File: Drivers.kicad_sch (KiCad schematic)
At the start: 15 parts, among them IC1 A3909GLNTR-T, IC2 A3909GLNTR-T, IC3 A3909GLNTR-T, IC4 A3909GLNTR-T, J1 7 Seg Out, J3 Logic I/O, U1 74HC595, U2 74HC595

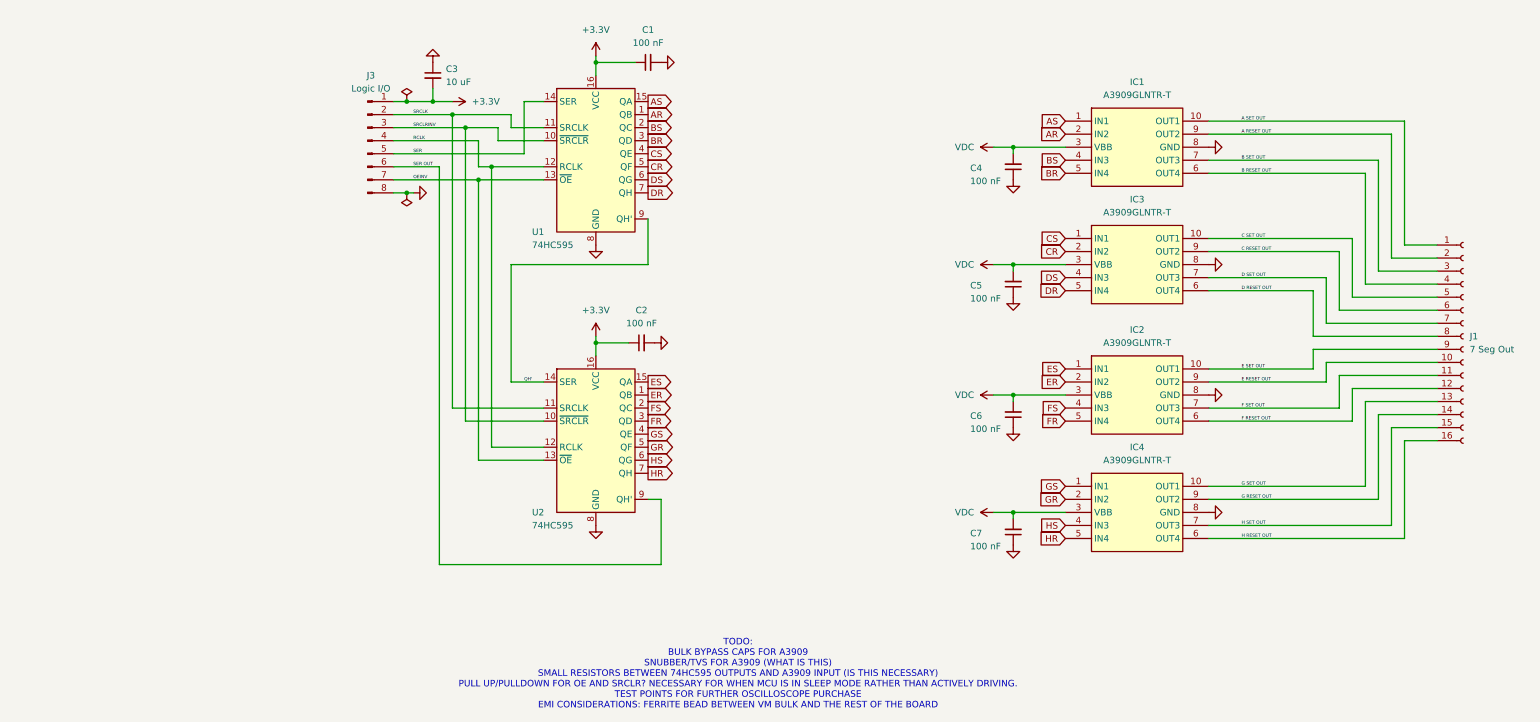
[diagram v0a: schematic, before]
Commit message: Pullup/pulldowns Footprints
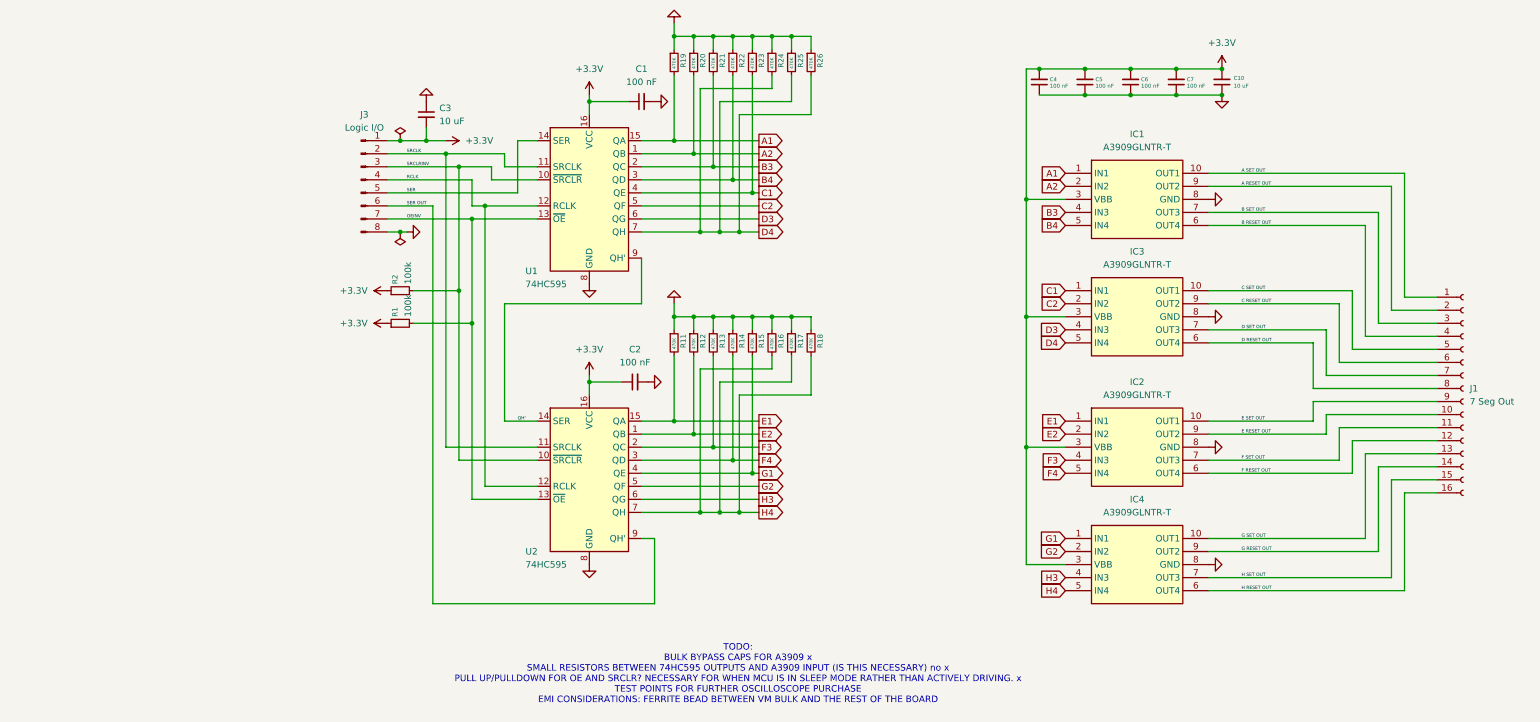
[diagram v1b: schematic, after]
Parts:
- added C10: 10 uF, symbol Device:C_Small
- added R1, R2: 100k, symbol Device:R_Small
- added R11, R12, R13, R14, R15, R16, R17, R18, R19, R20, R21, R22, R23, R24, R25, R26: 470K, symbol Device:R_Small
- IC1, IC2, IC3, IC4: symbol Drivers:A3909GLNTR-T -> A3909GLNTR-T:A3909GLNTR-T
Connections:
- net VDC is gone; now on net +3.3V: C4.2, C5.2, C6.2, C7.2, IC1.3 (VBB), IC2.3 (VBB), IC3.3 (VBB), IC4.3 (VBB)
- net +3.3V: now also C10.2, R1.1, R2.1
- net GND: now also C10.1, R11.1, R12.1, R13.1, R14.1, R15.1, R16.1, R17.1, R18.1, R19.1, R20.1, R21.1, R22.1, R23.1, R24.1, R25.1, R26.1
- net OEINV: now also R1.2
- net SRCLRINV: now also R2.2
- net AR renamed A2
- net A2: now also R20.2
- net AS renamed A1
- net A1: now also R19.2
- net BR renamed B4
- net B4: now also R22.2
- net BS renamed B3
- net B3: now also R21.2
- net CR renamed C2
- net CS renamed C1
- net C1: now also R23.2
- net DR renamed D4
- net D4: now also R24.2, R25.2, R26.2
- net DS renamed D3
- net ER renamed E2
- net E2: now also R12.2
- net ES renamed E1
- net E1: now also R11.2
- net FR renamed F4
- net F4: now also R14.2
- net FS renamed F3
- net F3: now also R13.2
- net GR renamed G2
- net GS renamed G1
- net G1: now also R15.2
- net HR renamed H4
- net H4: now also R16.2, R17.2, R18.2
- net HS renamed H3
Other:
- note added: "TODO: BULK BYPASS CAPS FOR A3909 x SMALL RESISTORS BETWEEN 74HC595 OUTPUTS AND A3909 INPUT (IS THIS NECESSARY) no x PULL UP/PULLDOWN FOR OE AND SRCLR? NECESSARY FOR WHEN MCU IS IN SLEEP MODE RATHER THAN ACTIVELY DRIVING. x TEST POINTS FOR FURTHER OSCILLOSCOPE PURCHASE EMI CONSIDERATIONS: FERRITE BEAD BETWEEN VM BULK AND THE REST OF THE BOARD"
- note removed: "TODO: BULK BYPASS CAPS FOR A3909 SNUBBER/TVS FOR A3909 (WHAT IS THIS) SMALL RESISTORS BETWEEN 74HC595 OUTPUTS AND A3909 INPUT (IS THIS NECESSARY) PULL UP/PULLDOWN FOR OE AND SRCLR? NECESSARY FOR WHEN MCU IS IN SLEEP MODE RATHER THAN ACTIVELY DRIVING. TEST POINTS FOR FURTHER OSCILLOSCOPE PURCHASE EMI CONSIDERATIONS: FERRITE BEAD BETWEEN VM BULK AND THE REST OF THE BOARD"
- moved on the sheet: C1, C2, C3, C4, IC1, IC2, IC3, IC4, J1, J3, U1, U2

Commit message: Fin drivers, start voltage reg
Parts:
- added TP1, TP2, TP3, TP4: TestPoint, symbol Connector:TestPoint
- C1, C2, C4, C5, C6, C7: footprint (none) -> Capacitor_SMD:C_01005_0402Metric
- C10, C3: footprint (none) -> Capacitor_SMD:C_0805_2012Metric
- J1: footprint (none) -> Connector_PinHeader_2.54mm:PinHeader_1x16_P2.54mm_Vertical
- J3: footprint (none) -> Connector_PinHeader_2.54mm:PinHeader_1x08_P2.54mm_Vertical
- R1, R11, R12, R13, R14, R15, R16, R17, R18, R19, R2, R20, R21, R22, R23, R24, R25, R26: footprint (none) -> Resistor_SMD:R_0402_1005Metric
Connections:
- net +3.3V: now also TP1.1; no longer C10.2, C4.2, C5.2, C6.2, C7.2, IC1.3 (VBB), IC2.3 (VBB), IC3.3 (VBB), IC4.3 (VBB)
- net GND: now also TP3.1
- net SER: now also TP2.1
- new net VDC: C10.2, C4.2, C5.2, C6.2, C7.2, IC1.3 (VBB), IC2.3 (VBB), IC3.3 (VBB), IC4.3 (VBB), TP4.1
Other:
- note removed: "TODO: BULK BYPASS CAPS FOR A3909 x SMALL RESISTORS BETWEEN 74HC595 OUTPUTS AND A3909 INPUT (IS THIS NECESSARY) no x PULL UP/PULLDOWN FOR OE AND SRCLR? NECESSARY FOR WHEN MCU IS IN SLEEP MODE RATHER THAN ACTIVELY DRIVING. x TEST POINTS FOR FURTHER OSCILLOSCOPE PURCHASE EMI CONSIDERATIONS: FERRITE BEAD BETWEEN VM BULK AND THE REST OF THE BOARD"
